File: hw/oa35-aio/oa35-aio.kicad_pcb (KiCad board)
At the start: 6 copper layers, 36 x 36 mm, 283 parts, among them J1 TYPE-C-31-M-12, J10 M1A, J11 M1B, J12 M1C, J13 M2A, J14 M2B, J15 M2C, J16 M3A, J17 M3B, J18 M3C, J19 M4A, J2 SM06B-SRSS-TB, J20 M4B, J21 M4C, J3 BAT+, J4 BAT-, P1 +5V, P10 TX6, P11 RX1, P12 TX1, P13 LED, P14 BZ-, P15 BZ+, P16 RSSI, P17 SCL, P18 SDA, P19 +3V3, P2 GND, P20 GND, P21 VBAT, P22 GND, P3 RX2, P4 TX2, P5 +5V, P6 GND, P7 RX4, P8 TX4, P9 RX6, Q1 2N7002, U1 INA186A3IDCKR, U10 USBLC6-2SC6, U2 LMR51430YFDDCR, U20 AT32F421G8U7, U21 NSG2065Q, U3 LMR51430YFDDCR, U30 AT32F421G8U7, U31 NSG2065Q, U4 LP5912-3.3DRVR, U40 AT32F421G8U7, U41 NSG2065Q, U5 TLV76733DRVR, U50 AT32F421G8U7, U51 NSG2065Q, U6 STM32F722RET6, U7 ICM-42688-P, U8 BMP280, U9 W25Q128JVSIQ, Y1 8MHz

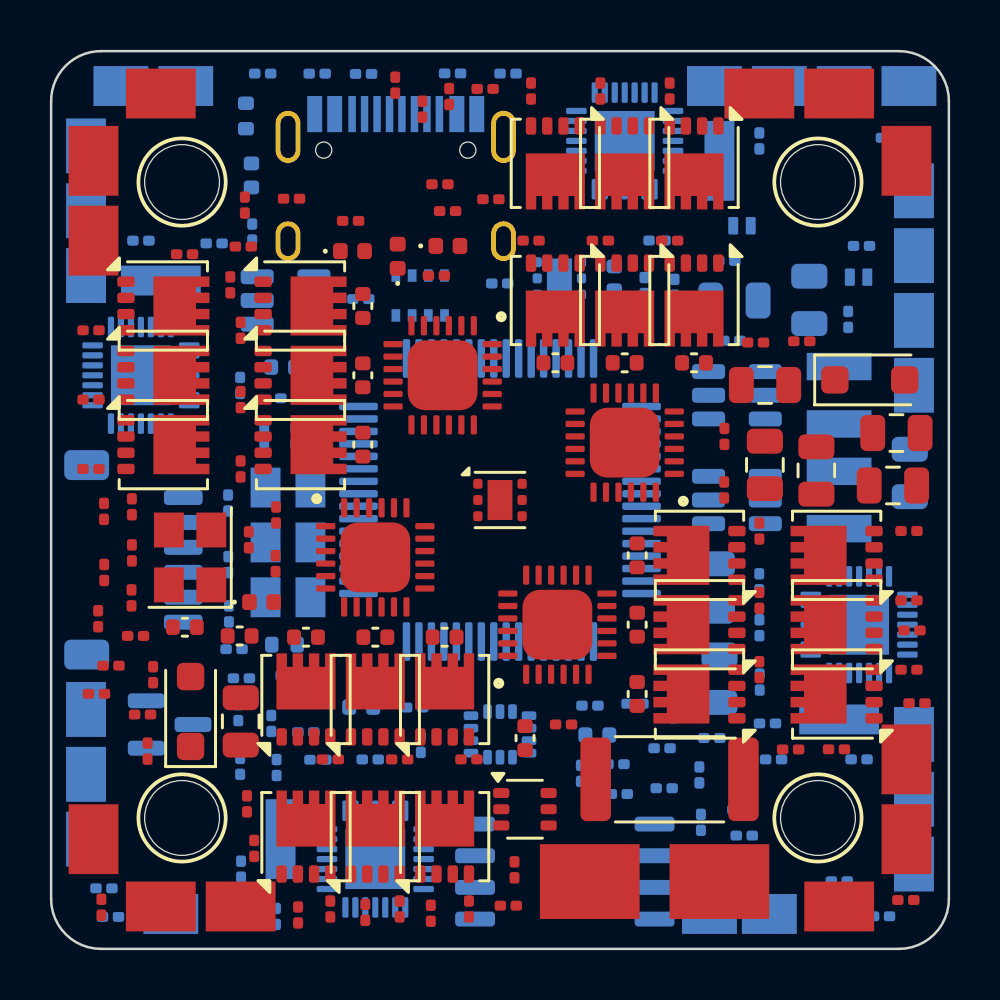
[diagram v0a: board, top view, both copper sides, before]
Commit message: OA35-AIO: all 200 signal nets connected
First routing where nothing is unroutable: 9668 segments, 302 vias, no net
left in pieces.  The 206 unconnected pads are GND and VBAT, which are planes
and get their copper from the pours.

Not legal yet -- 26078 cells still carry two nets closer than the clearance
allows.  That is what the remaining negotiation iterations are for.

Co-Authored-By: Claude Opus 5 <noreply@anthropic.com>
Claude-Session: https://claude.ai/code/session_013J1rgXZWykCJN7jVVS67P2
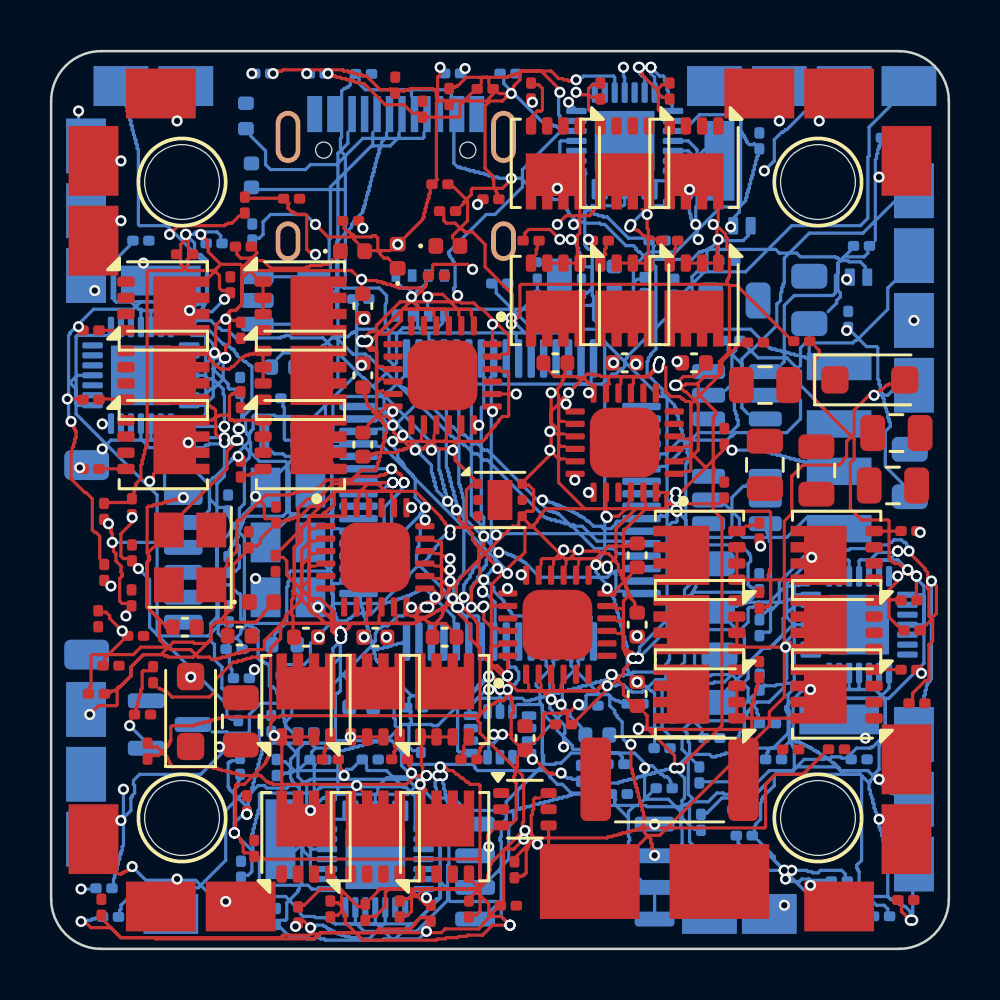
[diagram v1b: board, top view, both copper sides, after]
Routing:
- net +3V3: track 0.00 -> 125.1 mm, vias 0 -> 15
- net +5V: track 0.00 -> 110.5 mm, vias 0 -> 8
- net +3V3E: track 0.00 -> 93.8 mm
- net +10V: track 0.00 -> 72.0 mm, vias 0 -> 4
- net PH_C_2: track 0.00 -> 53.5 mm, vias 0 -> 4
- net FBC_2: track 0.00 -> 48.7 mm, vias 0 -> 5
- net PH_C_4: track 0.00 -> 46.2 mm, vias 0 -> 5
- net FBCOM_1: track 0.00 -> 46.0 mm
- net VBAT_IN: track 0.00 -> 44.5 mm, vias 0 -> 3
- net FBC_1: track 0.00 -> 43.6 mm, vias 0 -> 3
- net PH_B_2: track 0.00 -> 40.2 mm, vias 0 -> 6
- net PH_A_2: track 0.00 -> 39.8 mm, vias 0 -> 5
- net I2C_SCL: track 0.00 -> 39.4 mm
- net PH_B_4: track 0.00 -> 39.4 mm, vias 0 -> 5
- net I2C_SDA: track 0.00 -> 39.3 mm, vias 0 -> 4
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
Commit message: OA35-AIO: routing iteration 2, conflicts 26078 -> 19956
Co-Authored-By: Claude Opus 5 <noreply@anthropic.com>
Claude-Session: https://claude.ai/code/session_013J1rgXZWykCJN7jVVS67P2
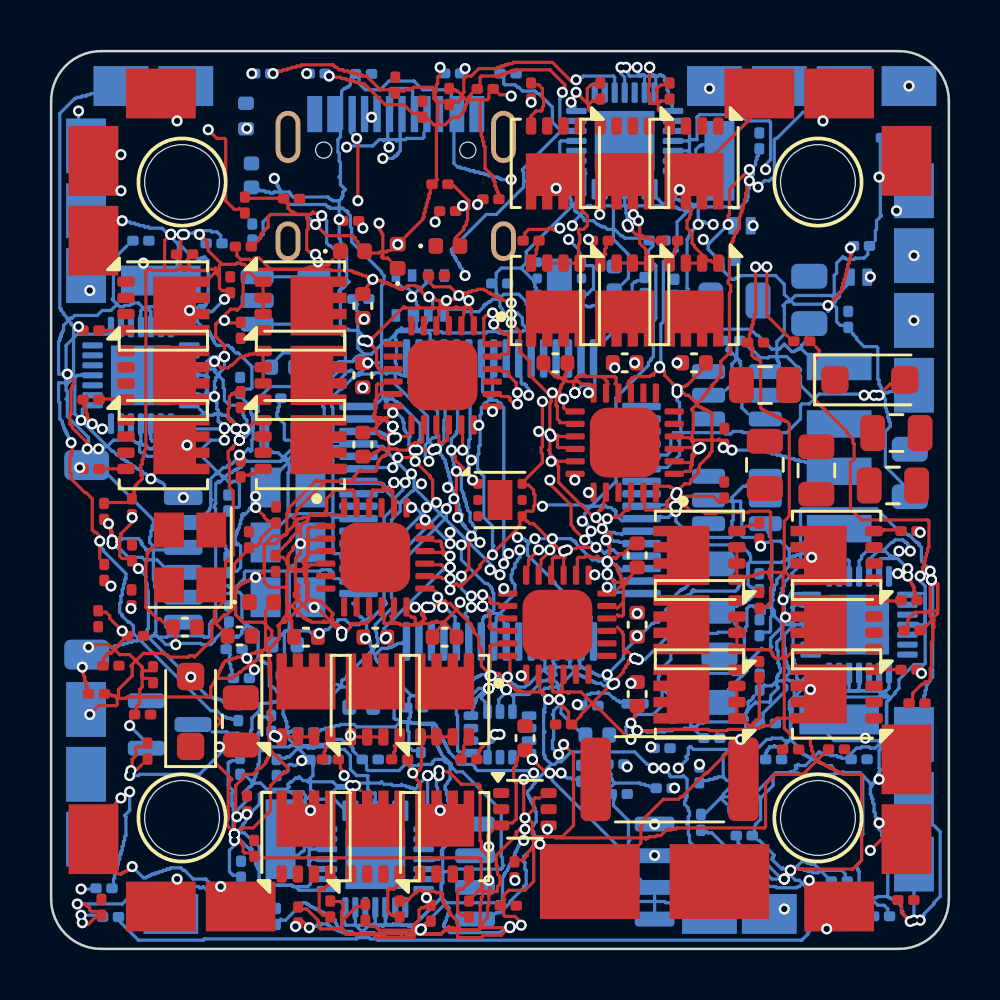
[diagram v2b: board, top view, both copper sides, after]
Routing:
- net PH_B_4: track 39.4 -> 54.2 mm, vias 5 -> 9
- net +3V3E: track 93.8 -> 104.1 mm, vias 0 -> 4
- net PAD_BZ-: track 30.0 -> 39.7 mm, vias 0 -> 2
- net FBC_1: track 43.6 -> 52.3 mm, vias 3 -> 5
- net PH_A_1: track 31.1 -> 38.7 mm
- net UART2_RX: track 37.6 -> 45.1 mm
- net CH_3: track 18.1 -> 25.4 mm
- net VDDA_3: track 17.2 -> 24.1 mm
- net CH_2: track 15.6 -> 22.0 mm
- net PH_A_4: track 27.6 -> 33.5 mm
- net UART1_RX: track 36.6 -> 42.4 mm
- net FBC_2: track 48.7 -> 54.4 mm, vias 5 -> 4
- net PH_C_3: track 33.3 -> 38.9 mm
- net HSE_OUT: track 14.2 -> 19.7 mm, vias 1 -> 2
- net I2C_SDA: track 39.3 -> 44.5 mm, vias 4 -> 5
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
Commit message: OA35-AIO: routing iteration 3
Co-Authored-By: Claude Opus 5 <noreply@anthropic.com>
Claude-Session: https://claude.ai/code/session_013J1rgXZWykCJN7jVVS67P2
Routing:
- net UART2_RX: track 45.1 -> 60.3 mm, vias 3 -> 4
- net NRST_4: track 18.6 -> 31.0 mm, vias 2 -> 3
- net LED1: track 18.6 -> 30.5 mm, vias 1 -> 2
- net PH_B_3: track 29.4 -> 41.0 mm
- net FBB_1: track 34.8 -> 45.0 mm, vias 1 -> 3
- net BL_3: track 24.5 -> 34.2 mm
- net FBA_3: track 29.6 -> 39.2 mm
- net HSE_IN: track 19.0 -> 28.4 mm
- net PH_B_4: track 54.2 -> 44.9 mm
- net PH_C_1: track 33.2 -> 42.2 mm, vias 4 -> 5
- net CC2: track 26.7 -> 35.7 mm, vias 3 -> 2
- net BOOTA_3: track 11.5 -> 20.3 mm, vias 0 -> 2
- net UART1_TX: track 37.3 -> 45.7 mm
- net FLASH_MOSI: track 9.35 -> 17.6 mm
- net PH_C_2: track 57.3 -> 64.6 mm, vias 4 -> 6
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
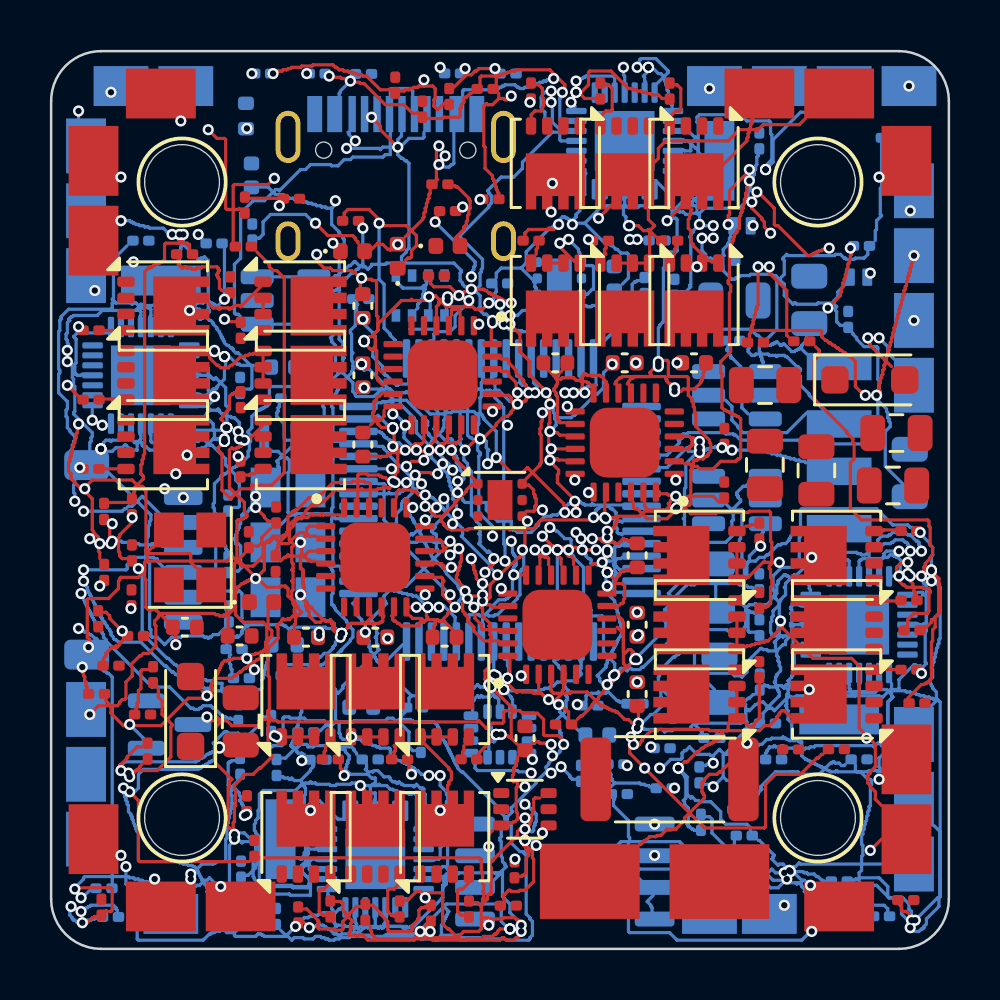
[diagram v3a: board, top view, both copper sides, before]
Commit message: OA35-AIO: re-route with the legal-by-construction router
Co-Authored-By: Claude Opus 5 <noreply@anthropic.com>
Claude-Session: https://claude.ai/code/session_013J1rgXZWykCJN7jVVS67P2
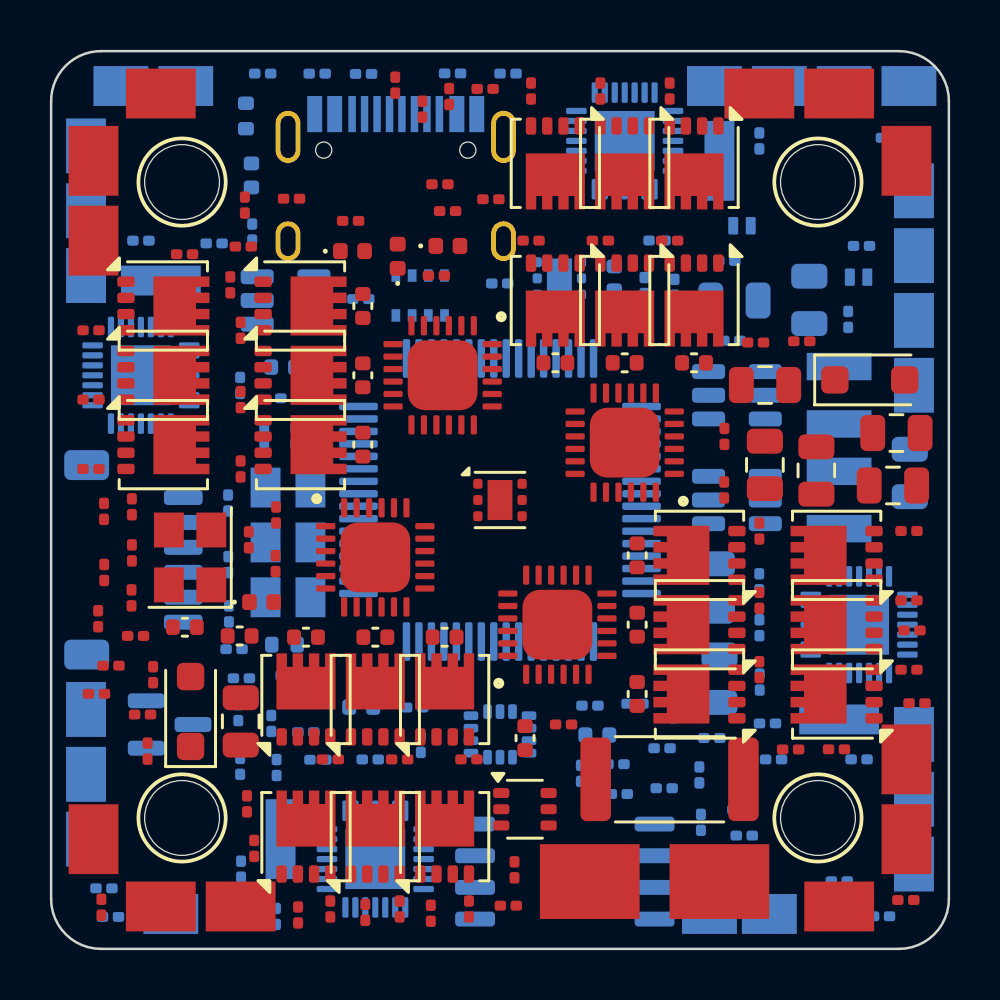
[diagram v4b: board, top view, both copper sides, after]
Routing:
- net +3V3: track 135.1 -> 0.00 mm, vias 19 -> 0
- net +5V: track 111.9 -> 0.00 mm, vias 13 -> 0
- net +3V3E: track 107.1 -> 0.00 mm, vias 5 -> 0
- net +10V: track 69.8 -> 0.00 mm, vias 10 -> 0
- net PH_C_2: track 64.6 -> 0.00 mm, vias 6 -> 0
- net UART2_RX: track 60.3 -> 0.00 mm, vias 4 -> 0
- net FBC_2: track 55.8 -> 0.00 mm, vias 6 -> 0
- net FBC_1: track 53.0 -> 0.00 mm, vias 4 -> 0
- net PH_C_4: track 52.1 -> 0.00 mm, vias 6 -> 0
- net FBCOM_1: track 49.2 -> 0.00 mm, vias 2 -> 0
- net I2C_SCL: track 46.9 -> 0.00 mm, vias 7 -> 0
- net VBAT_IN: track 46.6 -> 0.00 mm, vias 7 -> 0
- net UART1_TX: track 45.7 -> 0.00 mm, vias 4 -> 0
- net FBB_1: track 45.0 -> 0.00 mm, vias 3 -> 0
- net PH_B_4: track 44.9 -> 0.00 mm, vias 9 -> 0
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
